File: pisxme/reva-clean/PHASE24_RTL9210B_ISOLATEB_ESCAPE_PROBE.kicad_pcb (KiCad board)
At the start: 6 copper layers, 100.1 x 55.1 mm, 15 parts, among them J1 M.2 Socket 3 M-key 2280, U1 RTL9210B-CG, U2 W25Q128_SPI_FLASH, Y1 XTAL_25MHz

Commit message: phase24: narrow ISOLATEB local reroute constraint
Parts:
- moved TP_ISO 4.03 mm to (105.0, 78.5)
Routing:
- net ISOLATEB: track 16.3 -> 10.8 mm
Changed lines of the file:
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@@
-	(footprint ""
-		(layer "F.Cu")
-		(at 107 82)
-		(property "Reference" "TP_ISO"
-			(at 0 0 0)
-			(layer "F.SilkS")
-			(effects
-				(font
-					(size 1.27 1.27)
-				)
-			)
-		)
-		(property "Value" "ISOLATEB_HANDOFF"
-			(at 0 0 0)
-			(layer "F.Fab")
-			(effects
-				(font
-					(size 1.27 1.27)
-				)
-			)
-		)
-		(property "Datasheet" ""
-			(at 0 0 0)
-			(layer "F.Fab")
-			(hide yes)
-			(effects
-				(font
-					(size 1.27 1.27)
-				)
-			)
-		)
-		(property "Description" ""
-			(at 0 0 0)
-			(layer "F.Fab")
-			(hide yes)
-			(effects
-				(font
-					(size 1.27 1.27)
-				)
-			)
-		)
-		(duplicate_pad_numbers_are_jumpers no)
-		(pad "1" smd circle
-			(at 0 0)
-			(size 0.8 0.8)
-			(layers "F.Cu")
-			(net "ISOLATEB")
-		)
-		(embedded_fonts no)
-	)
 	(footprint ""
 		(layer "F.Cu")
@@
 			(layers "F.Cu" "F.Mask" "F.Paste")
 			(net "XTAL_OUT")
+		)
+		(embedded_fonts no)
+	)
+	(footprint ""
+		(layer "F.Cu")
+		(at 105 78.5)
+		(property "Reference" "TP_ISO"
+			(at 0 0 0)
+			(layer "F.SilkS")
+			(effects
+				(font
+					(size 1.27 1.27)
+				)
+			)
+		)
+		(property "Value" "ISOLATEB_HANDOFF"
+			(at 0 0 0)
+			(layer "F.Fab")
+			(effects
+				(font
+					(size 1.27 1.27)
+				)
+			)
+		)
+		(property "Datasheet" ""
+			(at 0 0 0)
+			(layer "F.Fab")
+			(hide yes)
+			(effects
+				(font
+					(size 1.27 1.27)
+				)
+			)
+		)
+		(property "Description" ""
+			(at 0 0 0)
+			(layer "F.Fab")
+			(hide yes)
+			(effects
+				(font
+					(size 1.27 1.27)
+				)
+			)
+		)
+		(duplicate_pad_numbers_are_jumpers no)
+		(pad "1" smd circle
+			(at 0 0)
+			(size 0.8 0.8)
+			(layers "F.Cu")
+			(net "ISOLATEB")
 		)
 		(embedded_fonts no)
@@
 	)
 	(segment
+		(start 101.8 74.6)
+		(end 101.8 78.5)
+		(width 0.2)
+		(layer "F.Cu")
+		(net "ISOLATEB")
+	)
+	(segment
+		(start 99.2 74.6)
+		(end 101.8 74.6)
+		(width 0.2)
+		(layer "F.Cu")
+		(net "ISOLATEB")
+	)
+	(segment
 		(start 99.2 73.5)
-		(end 99.2 77)
+		(end 99.2 74.6)
 		(width 0.2)
 		(layer "F.Cu")
@@
 	)
 	(via
-		(at 99.2 77)
+		(at 105 78.5)
 		(size 0.6)
 		(drill 0.3)
@@
 	)
 	(via
-		(at 107 82)
+		(at 101.8 78.5)
 		(size 0.6)
 		(drill 0.3)
@@
 	)
 	(segment
-		(start 99.2 77)
-		(end 107 77)
+		(start 101.8 78.5)
+		(end 105 78.5)
 		(width 0.2)
 		(layer "B.Cu")
-		(net "ISOLATEB")
-	)
-	(segment
-		(start 107 77)
-		(end 107 82)
-		(width 0.2)
-		(layer "B.Cu")

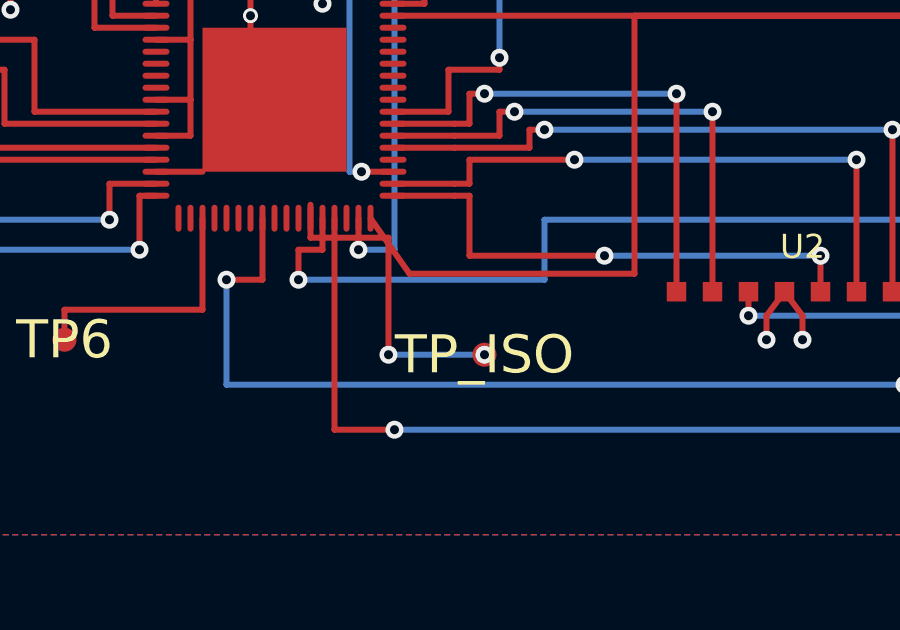
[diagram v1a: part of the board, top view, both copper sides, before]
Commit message: phase24: preserve left-dogbone ISOLATEB probe
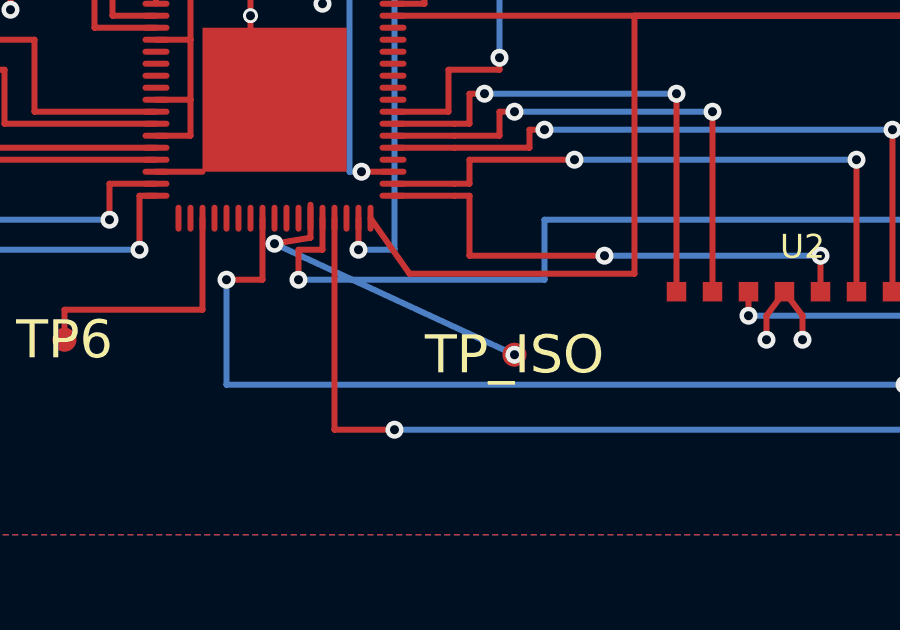
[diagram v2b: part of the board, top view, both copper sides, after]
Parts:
- moved TP_ISO 1.00 mm to (106.0, 78.5)
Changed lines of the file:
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@@
-		(embedded_fonts no)
-	)
-	(footprint ""
-		(layer "F.Cu")
-		(at 105 78.5)
-		(property "Reference" "TP_ISO"
-			(at 0 0 0)
-			(layer "F.SilkS")
-			(effects
-				(font
-					(size 1.27 1.27)
-				)
-			)
-		)
-		(property "Value" "ISOLATEB_HANDOFF"
-			(at 0 0 0)
-			(layer "F.Fab")
-			(effects
-				(font
-					(size 1.27 1.27)
-				)
-			)
-		)
-		(property "Datasheet" ""
-			(at 0 0 0)
-			(layer "F.Fab")
-			(hide yes)
-			(effects
-				(font
-					(size 1.27 1.27)
-				)
-			)
-		)
-		(property "Description" ""
-			(at 0 0 0)
-			(layer "F.Fab")
-			(hide yes)
-			(effects
-				(font
-					(size 1.27 1.27)
-				)
-			)
-		)
-		(duplicate_pad_numbers_are_jumpers no)
-		(pad "1" smd circle
-			(at 0 0)
-			(size 0.8 0.8)
-			(layers "F.Cu")
-			(net "ISOLATEB")
-		)
 		(embedded_fonts no)
 	)
@@
 			(layers "F.Cu" "F.Mask" "F.Paste")
 			(net "RTL_3V3")
+		)
+		(embedded_fonts no)
+	)
+	(footprint ""
+		(layer "F.Cu")
+		(at 106 78.5)
+		(property "Reference" "TP_ISO"
+			(at 0 0 0)
+			(layer "F.SilkS")
+			(effects
+				(font
+					(size 1.27 1.27)
+				)
+			)
+		)
+		(property "Value" "ISOLATEB_HANDOFF"
+			(at 0 0 0)
+			(layer "F.Fab")
+			(effects
+				(font
+					(size 1.27 1.27)
+				)
+			)
+		)
+		(property "Datasheet" ""
+			(at 0 0 0)
+			(layer "F.Fab")
+			(hide yes)
+			(effects
+				(font
+					(size 1.27 1.27)
+				)
+			)
+		)
+		(property "Description" ""
+			(at 0 0 0)
+			(layer "F.Fab")
+			(hide yes)
+			(effects
+				(font
+					(size 1.27 1.27)
+				)
+			)
+		)
+		(duplicate_pad_numbers_are_jumpers no)
+		(pad "1" smd circle
+			(at 0 0)
+			(size 0.8 0.8)
+			(layers "F.Cu")
+			(net "ISOLATEB")
 		)
 		(embedded_fonts no)
@@
 	)
 	(segment
-		(start 101.8 74.6)
-		(end 101.8 78.5)
-		(width 0.2)
-		(layer "F.Cu")
-		(net "ISOLATEB")
-	)
-	(segment
-		(start 99.2 74.6)
-		(end 101.8 74.6)
-		(width 0.2)
-		(layer "F.Cu")
-		(net "ISOLATEB")
-	)
-	(segment
 		(start 99.2 73.5)
 		(end 99.2 74.6)
@@
 		(net "ISOLATEB")
 	)
+	(segment
+		(start 99.2 74.6)
+		(end 98 74.8)
+		(width 0.2)
+		(layer "F.Cu")
+		(net "ISOLATEB")
+	)
 	(via
-		(at 105 78.5)
+		(at 98 74.8)
 		(size 0.6)
 		(drill 0.3)
@@
 	)
 	(via
-		(at 101.8 78.5)
+		(at 106 78.5)
 		(size 0.6)
 		(drill 0.3)
@@
 	)
 	(segment
-		(start 101.8 78.5)
-		(end 105 78.5)
+		(start 98 74.8)
+		(end 106 78.5)
 		(width 0.2)
 		(layer "B.Cu")
